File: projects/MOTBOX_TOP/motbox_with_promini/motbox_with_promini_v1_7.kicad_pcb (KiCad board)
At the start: 2 copper layers, 81.9 x 65 mm, 44 parts, among them J1 JST_XH_2pin, J2 JST_XH_3pin, J3 Conn_01x02, J4 JST_XH_4pin, J5 JST_XH_3pin, J6 JST_XH_3pin, J7 JST_XH_2pin, J8 Conn_02x03_Odd_Even, J9 Conn_01x02, U1 LM2576R-5.0, U2 L293D, U3 ATmega328P-AU, Y1 ABLS-16.000MHZ-B4-T

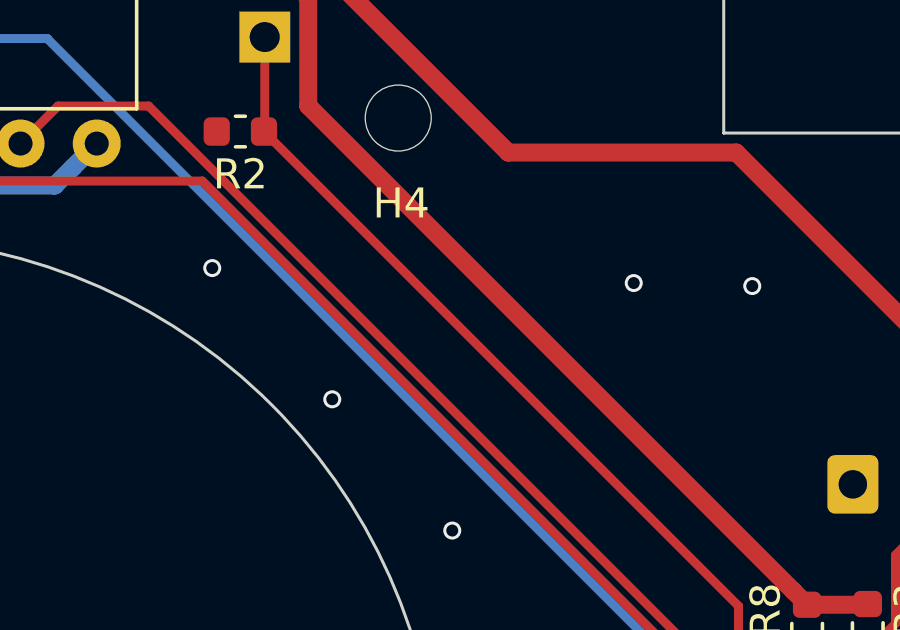
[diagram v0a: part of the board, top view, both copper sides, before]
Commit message: For transparent cable detection
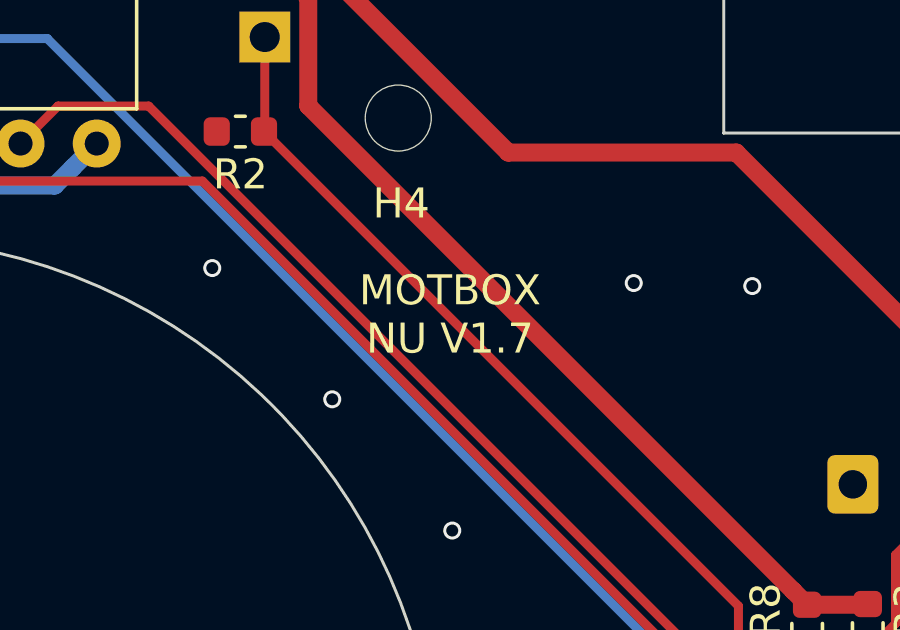
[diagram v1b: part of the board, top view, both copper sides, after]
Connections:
- net /Atmega328p_board/A2 renamed /A2
- net /Atmega328p_board/A3 renamed /A3
- net /Atmega328p_board/A4 renamed /A4
- net /Atmega328p_board/A5 renamed /A5
- net /Atmega328p_board/A6 renamed /A6
- net /Atmega328p_board/RESET renamed /RESET
- net /Atmega328p_board/SCK renamed /SCK
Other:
- board text added: "+12"
- board text added: "CL"
- board text added: "MOTBOX NU V1.7"
- board text added: "OP"
- board text added: "TS GND"
- board text removed: "+12V"
- board text removed: "OP CL DN"
- board text removed: "SW+OBS LED GND"
